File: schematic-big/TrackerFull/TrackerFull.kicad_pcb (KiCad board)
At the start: 2 copper layers, 41.1 x 61.5 mm, 59 parts, among them J1 Conn_01x05_Male, J2 MUC-20PFFR-JS7001, J3 Battery, J4 78646-3001, Q2 DMG2305UXQ, Q3 DMG2305UXQ, SW1 PTS647SK38SMTR2LFS, U2 LIS3DSH, U3 ATtiny85-20PU, U4 MCP73831-2-OT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

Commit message: schematics update
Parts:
- removed C13: 100nF, Capacitor_SMD:C_0402_1005Metric
- removed C18: 22uF, Capacitor_SMD:C_0603_1608Metric
- added U1: TLV62585PDRLR, imported:SOT50P160X60-6N, F.Cu at (191.0, 70.4)
- C17: footprint Capacitor_SMD:C_0603_1608Metric -> Capacitor_SMD:C_0805_2012Metric
- L2: value MDWK4040T3R3MM -> 1uH; footprint Inductor_SMD:L_Taiyo-Yuden_MD-4040 -> Inductor_SMD:L_Vishay_IHLP-2020
- R1: footprint Resistor_SMD:R_0805_2012Metric_Pad1.15x1.40mm_HandSolder -> Resistor_SMD:R_0603_1608Metric
- R13: value 43K -> 562K
- R14: value 10K -> 100K; footprint Resistor_SMD:R_0805_2012Metric_Pad1.15x1.40mm_HandSolder -> Resistor_SMD:R_0603_1608Metric
- moved U8 36.1 mm to (156.1, 73.0)
- moved C17 4.49 mm to (197.7, 68.7), turned to 180 degrees
- moved L2 2.67 mm to (195.7, 72.6)
- moved D3 0.73 mm to (201.2, 71.9)
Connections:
- J2 pad 1: (no net) -> /+5V
- L2 pad 1: Net-(C13-Pad1) -> Net-(L2-Pad1)
- U8 pad 1: GNDREF -> (no net)
- U8 pad 2: Net-(C13-Pad1) -> (no net)
- U8 pad 3: /+5V -> (no net)
- U8 pad 4: Net-(R13-Pad2) -> (no net)
- U8 pad 5: /+5V -> (no net)
- U8 pad 6: Net-(C13-Pad2) -> (no net)
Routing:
- net Net-(C13-Pad1): track 5.37 -> 0.00 mm
- net Net-(L2-Pad1): track 0.00 -> 4.20 mm
- net /+5V: track 67.9 -> 71.2 mm, vias 11 -> 13
- net Net-(C13-Pad2): track 1.96 -> 0.00 mm
- net /CHARGER_STAT: track 56.0 -> 56.6 mm
- net /APW_OUT: track 25.9 -> 26.5 mm
- net Net-(R13-Pad2): track 3.63 -> 4.22 mm
- net GNDREF: track 142.6 -> 142.8 mm, vias 43 -> 42

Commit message: replaced attiny
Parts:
- removed C4: 150nF, Capacitor_SMD:C_0402_1005Metric
- removed C5: 10uF, Capacitor_SMD:C_0603_1608Metric
- removed R11: 470, Resistor_SMD:R_0402_1005Metric
- removed U3: ATtiny85-20PU, Package_DIP:DIP-8_W7.62mm
- added C13: 150nF, Capacitor_SMD:C_0402_1005Metric, F.Cu at (190.1, 76.5)
- added C18: 10uF, Capacitor_SMD:C_0603_1608Metric, F.Cu at (192.6, 76.7)
- added J5: Conn_01x04_Male, Connector_PinHeader_2.54mm:PinHeader_1x04_P2.54mm_Vertical, B.Cu at (195.9, 68.4)
- added R2: 470, Resistor_SMD:R_0402_1005Metric, F.Cu at (188.3, 72.8)
- Q2, R1: moved to B.Cu
- U7: value MIC5232-2.5YD5 -> MIC5232-2.8YD5
- U8: value AP62301WU-7 -> ATtiny861A-MU; footprint Package_TO_SOT_SMD:TSOT-23-6 -> Package_DFN_QFN:QFN-32-1EP_5x5mm_P0.5mm_EP3.1x3.1mm
- moved U8 36.0 mm to (192.1, 72.7), turned to 270 degrees
- moved C16 22.6 mm to (170.0, 80.5), turned to 270 degrees
- moved U7 21.8 mm to (190.8, 88.5), turned to 0 degrees
- moved R13 21.5 mm to (171.5, 70.9), turned to 90 degrees
- moved C3 20.0 mm to (191.5, 85.8), turned to 180 degrees
- moved L2 19.5 mm to (176.3, 70.9), turned to 270 degrees
- moved C11 19.3 mm to (170.0, 68.6)
- moved U1 19.0 mm to (172.1, 68.2), turned to 180 degrees
- moved R14 18.4 mm to (171.7, 73.2), turned to 0 degrees
- moved C2 18.4 mm to (191.0, 84.4), turned to 180 degrees
- moved C19 18.4 mm to (188.0, 88.7)
- moved D3 18.2 mm to (183.2, 73.7), turned to 180 degrees
- moved R3 18.0 mm to (188.3, 74.7), turned to 270 degrees
- moved C17 17.6 mm to (180.1, 70.1), turned to 90 degrees
- moved U2 16.4 mm to (190.7, 81.8), turned to 180 degrees
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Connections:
- net /V_BAT renamed /BATTERY_IN
- R3 pad 1: /PWR_CTRL -> Net-(R3-Pad1)
- R3 pad 2: Net-(R3-Pad2) -> /LED_CTL
- U8 pad 4: (no net) -> BAT_IN
- U8 pad 5: (no net) -> GNDREF
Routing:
- net GNDREF: track 142.8 -> 88.7 mm, vias 42 -> 10
- net /CHARGER_STAT: track 56.6 -> 16.7 mm
- net /ACCEL_INT2: track 30.2 -> 0.99 mm, vias 2 -> 0
- net /AVR_RST: track 26.7 -> 0.00 mm
- net /HST_TXD: track 24.3 -> 0.00 mm
- net /LED_CTL: track 20.8 -> 0.00 mm, vias 1 -> 0
- net /HST_RXD: track 19.2 -> 0.00 mm
- net /AVR_MOSI_SDA: track 19.1 -> 0.00 mm, vias 1 -> 0
- net /SIM_RST: track 19.6 -> 0.83 mm, vias 1 -> 0
- net /VSIM: track 18.3 -> 0.25 mm, vias 2 -> 0
- net /+5V: track 71.2 -> 88.8 mm, vias 13 -> 6
- net BAT_IN: track 67.8 -> 50.6 mm, vias 5 -> 3
- net /SIM_CLK: track 16.7 -> 0.00 mm, vias 1 -> 0
- net /SIM_IO: track 14.2 -> 0.51 mm, vias 1 -> 0
- net /ACCEL_INT1: track 12.9 -> 0.72 mm
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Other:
- board size 41.1 x 61.5 mm -> 32.8 x 61.5 mm

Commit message: replaced attiny
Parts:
- C1, C19, D3, U7: moved to B.Cu
- moved J2 16.3 mm to (192.3, 66.3), turned to 0 degrees
- moved C1 13.7 mm to (192.1, 98.4), turned to 90 degrees
- moved D2 13.1 mm to (195.3, 71.7), turned to 180 degrees
- moved U7 10.1 mm to (189.3, 98.5)
- moved R8 10.1 mm to (192.4, 71.6), turned to 0 degrees
- moved C19 9.72 mm to (186.5, 98.3)
- moved R10 7.63 mm to (189.0, 71.7), turned to 180 degrees
- moved D3 7.14 mm to (177.1, 69.9), turned to 270 degrees
- moved J5 6.35 mm to (195.9, 74.7), turned to 180 degrees
- moved Q2 4.83 mm to (182.5, 73.7)
- moved SW1 3.06 mm to (190.2, 75.4)
- moved U6 2.81 mm to (188.5, 92.6)
- moved R3 2.51 mm to (186.0, 75.7)
- moved R2 2.47 mm to (186.0, 73.7)
- moved R5 2.41 mm to (189.3, 80.8), turned to 180 degrees
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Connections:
- C15 pad 1: BAT_IN -> /VBAT
- C16 pad 1: BAT_IN -> /VBAT
- D1 pad 1: (no net) -> /AVR_SCK
- D1 pad 19: /ACCEL_CS -> (no net)
- D1 pad 2: (no net) -> /AVR_MOSI_SDA
- D1 pad 20: /ACCEL_SDO -> (no net)
- D1 pad 21: /ACCEL_SDA -> (no net)
- D1 pad 22: /ACCEL_SCL -> (no net)
- D1 pad 23: /AVR_SCK -> (no net)
- D1 pad 24: /AVR_MOSI_SDA -> (no net)
- R5 pad 1: /ACCEL_CS -> Net-(R5-Pad1)
- U2 pad 4: /ACCEL_SCL -> /AVR_SCK
- U2 pad 6: /ACCEL_SDA -> /AVR_MOSI_SDA
- U2 pad 7: /ACCEL_SDO -> Net-(R5-Pad1)
- U2 pad 8: /ACCEL_CS -> Net-(R5-Pad1)
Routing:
- net /HST_TXD: track 0.00 -> 22.6 mm
- net /AVR_MOSI_SDA: track 0.00 -> 22.6 mm, vias 0 -> 4
- net /+5V: track 88.8 -> 68.0 mm
- net /AVR_SCK: track 0.00 -> 19.3 mm, vias 0 -> 1
- net /AVR_RST: track 0.00 -> 18.8 mm, vias 0 -> 1
- net GNDREF: track 88.7 -> 105.9 mm, vias 10 -> 15
- net /UART1_RXD: track 0.00 -> 16.7 mm, vias 0 -> 1
- net /HST_RXD: track 0.00 -> 16.4 mm
- net BAT_IN: track 50.6 -> 66.4 mm
- net /UART1_TXD: track 0.00 -> 15.5 mm, vias 0 -> 1
- net /ACCEL_INT1: track 0.72 -> 12.8 mm, vias 0 -> 2
- net /LED_CTL: track 0.00 -> 11.1 mm, vias 0 -> 1
- net /2.5v: track 11.7 -> 21.6 mm, vias 0 -> 1
- net /ISP_MOSI: track 0.38 -> 9.25 mm
- net /BATTERY_IN: track 23.8 -> 15.1 mm
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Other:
- board size 32.8 x 61.5 mm -> 32.8 x 60.3 mm

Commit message: pcb layout
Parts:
- removed L1: LQG15HS5N1B02, Inductor_SMD:L_0402_1005Metric
- removed L3: LQG15HS1N8B02, Inductor_SMD:L_0402_1005Metric
- removed L5: 6.2nH, Inductor_SMD:L_0402_1005Metric
- added C4: 1.2 pF, Capacitor_SMD:C_0402_1005Metric, F.Cu at (181.4, 109.5)
- added R11: 0, Resistor_SMD:R_0402_1005Metric, B.Cu at (173.0, 85.9)
- added R4: 0, Resistor_SMD:R_0402_1005Metric, F.Cu at (186.0, 69.6)
- C1, C19, U7: moved to F.Cu
- C2, C3, R5, U2: moved to B.Cu
- C20: value 0.5 pF -> 6.8 pF
- L4: value 13nF -> 6.2nH
- R10: value 10K -> 100K; footprint Resistor_SMD:R_0805_2012Metric_Pad1.15x1.40mm_HandSolder -> Resistor_SMD:R_0603_1608Metric
- moved C19 12.8 mm to (190.5, 86.1), turned to 180 degrees
- moved R6 10.9 mm to (170.2, 100.4), turned to 0 degrees
- moved U7 9.69 mm to (190.7, 88.9), turned to 270 degrees
- moved C2 7.79 mm to (188.8, 79.3), turned to 270 degrees
- moved C3 7.45 mm to (188.5, 81.3), turned to 0 degrees
- moved C1 6.80 mm to (190.6, 91.7), turned to 180 degrees
- moved C20 6.00 mm to (177.4, 109.0), turned to 180 degrees
- moved FL1 4.55 mm to (180.4, 104.9), turned to 180 degrees
- moved U2 3.82 mm to (191.3, 80.3), turned to 270 degrees
- moved C9 3.44 mm to (182.2, 106.5), turned to 0 degrees
- moved L4 3.08 mm to (179.6, 109.0), turned to 180 degrees
- moved R5 2.30 mm to (189.5, 83.1)
- moved E1 1.52 mm to (181.6, 115.2)
- moved U5 0.36 mm to (181.4, 107.5), turned to 270 degrees
- turned Q3 to 180 degrees
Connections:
- C1 pad 2: GNDREF -> GNDD
- C13 pad 1: GNDREF -> GNDD
- C13 pad 2: BAT_IN -> /LOW_CURRENT
- C18 pad 1: GNDREF -> GNDD
- C18 pad 2: BAT_IN -> /LOW_CURRENT
- C19 pad 1: BAT_IN -> /LOW_CURRENT
- C19 pad 2: GNDREF -> GNDD
- C2 pad 1: GNDREF -> GNDD
- C20 pad 2: GNDREF -> GNDD
- C3 pad 1: GNDREF -> GNDD
- C9 pad 2: GNDREF -> GNDD
- D5 pad 1: GNDREF -> GNDD
- D5 pad 3: BAT_IN -> /LOW_CURRENT
- E1 pad 2: GNDREF -> GNDD
- E1 pad 3: GNDREF -> GNDD
- E1 pad 4: GNDREF -> GNDD
- E1 pad 5: GNDREF -> GNDD
- FL1 pad 2: GNDREF -> GNDD
- FL1 pad 3: GNDREF -> GNDD
- FL1 pad 5: GNDREF -> GNDD
- J4 pad C5: GNDREF -> GNDD
- J4 pad G1: GNDREF -> GNDD
- J4 pad G2: GNDREF -> GNDD
- J4 pad G3: GNDREF -> GNDD
- J4 pad G4: GNDREF -> GNDD
- J4 pad G5: GNDREF -> GNDD
- J4 pad G6: GNDREF -> GNDD
- L4 pad 1: Net-(C20-Pad1) -> /GPS_SIGNAL
- L4 pad 2: /GPS_SIGNAL -> Net-(C20-Pad1)
- Q3 pad 2: /BATTERY_IN -> BAT_IN
- Q3 pad 3: BAT_IN -> /BATTERY_IN
- R5 pad 2: GNDREF -> GNDD
- R6 pad 1: GNDREF -> GNDD
- SW1 pad 3: GNDREF -> GNDD
- SW1 pad 4: GNDREF -> GNDD
- U2 pad 10: GNDREF -> GNDD
- U2 pad 12: GNDREF -> GNDD
- U2 pad 13: GNDREF -> GNDD
- U2 pad 16: GNDREF -> GNDD
- U2 pad 5: GNDREF -> GNDD
- U5 pad 1: GNDREF -> GNDD
- U5 pad 4: GNDREF -> GNDD
- U7 pad 1: BAT_IN -> /LOW_CURRENT
- U7 pad 2: GNDREF -> GNDD
- U7 pad 3: BAT_IN -> /LOW_CURRENT
- U8 pad 18: BAT_IN -> /LOW_CURRENT
- U8 pad 21: GNDREF -> GNDD
- U8 pad 33: GNDREF -> GNDD
- U8 pad 4: BAT_IN -> /LOW_CURRENT
- U8 pad 5: GNDREF -> GNDD
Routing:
- net GNDD: track 0.00 -> 108.4 mm, vias 0 -> 5
- net /LOW_CURRENT: track 0.00 -> 55.7 mm, vias 0 -> 2
- net BAT_IN: track 66.4 -> 21.6 mm, vias 3 -> 2
- net GNDREF: track 105.9 -> 147.5 mm, vias 15 -> 12
- net /2.5v: track 21.6 -> 47.9 mm
- net /GPS_POWER: track 1.72 -> 9.04 mm
- net /AVR_SCK: track 19.3 -> 12.5 mm
- net /GPS_RF: track 0.01 -> 5.10 mm
- net /ACCEL_INT2: track 4.73 -> 8.92 mm, vias 0 -> 1
- net /ACCEL_INT1: track 12.8 -> 8.74 mm, vias 2 -> 1
- net /AVR_MOSI_SDA: track 22.6 -> 19.4 mm, vias 4 -> 2
- net Net-(R5-Pad1): track 2.61 -> 5.64 mm
- net Net-(C20-Pad1): track 3.60 -> 1.27 mm
- net Net-(C4-Pad2): track 0.00 -> 1.98 mm
- net /GPS_SIGNAL: track 0.88 -> 2.67 mm
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- added copper zone on B.Cu, net GNDD
- removed copper zone on B.Cu, net GNDREF
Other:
- board size 32.8 x 60.3 mm -> 32.8 x 62.3 mm
- net class low_current added: clearance 0.127, trace_width 0.25, via_dia 0.5, via_drill 0.3

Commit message: pcb layout
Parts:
- removed J4: 78646-3001, imported:MOLEX_78646-3001
- added J6: 78727-0001, simcard:Molex-78727-0001-0-0-MFG, B.Cu at (172.4, 94.4)
- added Q1: DMG2305UXQ, Package_TO_SOT_SMD:SOT-23, F.Cu at (181.4, 74.2)
- added R15: 100K, Resistor_SMD:R_0603_1608Metric, F.Cu at (184.0, 72.2)
- moved R10 22.8 mm to (166.4, 69.1), turned to 90 degrees
- moved J2 16.6 mm to (198.2, 81.8), turned to 270 degrees
- moved D2 13.2 mm to (193.6, 84.8), turned to 90 degrees
- moved R8 10.4 mm to (193.9, 81.9), turned to 270 degrees
- moved J5 9.92 mm to (188.3, 68.4), turned to 270 degrees
- moved SW1 3.58 mm to (193.1, 73.3)
- moved FL1 2.55 mm to (180.1, 107.5)
- moved R6 2.29 mm to (172.5, 100.4), turned to 180 degrees
- moved U6 1.78 mm to (190.3, 92.6)
- moved C17 1.63 mm to (181.4, 71.2), turned to 0 degrees
- moved U5 1.32 mm to (181.4, 108.8)
- moved C20 1.27 mm to (177.4, 110.3)
- moved C4 1.27 mm to (181.4, 110.8)
- moved C9 1.27 mm to (182.2, 107.7)
- moved E1 1.27 mm to (181.6, 116.5)
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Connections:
- D3 pad 1: BAT_IN -> /POWER_INPUT
- Q3 pad 2: BAT_IN -> /POWER_INPUT
- R1 pad 2: GNDREF -> BAT_IN
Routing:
- net GNDREF: track 147.5 -> 95.9 mm, vias 12 -> 11
- net /SIM_DETECT_LINE: track 0.00 -> 36.2 mm, vias 0 -> 1
- net GNDD: track 108.4 -> 86.6 mm, vias 5 -> 21
- net /+5V: track 68.3 -> 88.1 mm, vias 6 -> 9
- net /POWER_INPUT: track 0.00 -> 18.8 mm, vias 0 -> 2
- net /2.5v: track 47.9 -> 64.8 mm, vias 1 -> 3
- net /GPS_POWER: track 9.04 -> 22.5 mm
- net /GPS_RF: track 5.10 -> 17.4 mm
- net /LOW_CURRENT: track 55.7 -> 43.8 mm
- net BAT_IN: track 21.6 -> 12.3 mm, vias 2 -> 3
- net /SIM_IO: track 4.30 -> 12.0 mm
- net /SIM_CLK: track 2.04 -> 6.28 mm
- net /AVR_RST: track 18.8 -> 15.0 mm
- net /ISP_MOSI: track 9.25 -> 5.51 mm
- net /SIM_RST: track 3.70 -> 6.77 mm
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- added copper zone on B.Cu, net /CHARGER_PROG
- added copper zone on F.Cu, net GNDD
- added copper zone on F.Cu, net GNDREF
- removed copper zone on F.Cu, net BAT_IN
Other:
- board size 32.8 x 62.3 mm -> 32.8 x 63.9 mm
- net class Default: via_dia 0.8 -> 0.6; via_drill 0.4 -> 0.3
- net class low_current: via_dia 0.5 -> 0.6
- net class power: via_drill 0.6 -> 0.5

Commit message: rf
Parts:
- C1, C19, U7: moved to B.Cu
- moved R17 14.9 mm to (167.4, 81.6), turned to 270 degrees
- moved C19 9.72 mm to (182.9, 92.2), turned to 90 degrees
- moved C9 9.28 mm to (176.8, 100.2), turned to 180 degrees
- moved FL1 8.85 mm to (174.7, 100.5), turned to 90 degrees
- moved U5 8.81 mm to (176.8, 101.3)
- moved R7 7.37 mm to (169.7, 81.6), turned to 90 degrees
- moved R6 7.08 mm to (179.6, 100.8)
- moved U7 6.03 mm to (185.8, 92.4), turned to 0 degrees
- moved C1 5.66 mm to (186.0, 95.0), turned to 0 degrees
- moved D1 4.95 mm to (181.7, 88.8)
- moved C8 3.81 mm to (175.3, 77.2)
- moved C10 3.81 mm to (174.3, 77.2)
- moved C14 3.81 mm to (176.6, 76.7)
- moved C12 2.67 mm to (170.0, 76.5), turned to 180 degrees
- moved Q1 2.61 mm to (182.7, 76.5), turned to 270 degrees
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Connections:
- net Net-(C4-Pad2) renamed /ANT_OUT
- net Net-(FL1-Pad1) renamed /LNA_OUTPUT
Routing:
- net GNDD: track 86.6 -> 47.1 mm, vias 21 -> 18
- net /2.5v: track 64.8 -> 42.3 mm, vias 3 -> 2
- net Net-(D1-Pad5): track 3.07 -> 23.4 mm, vias 0 -> 2
- net /GPS_RF: track 17.4 -> 0.00 mm
- net /GPS_POWER: track 22.5 -> 5.92 mm
- net /+5V: track 88.1 -> 72.8 mm
- net Net-(D1-Pad9): track 2.51 -> 11.9 mm, vias 0 -> 2
- net /GPS_SIGNAL: track 2.62 -> 11.0 mm
- net /CHARGER_STAT: track 14.1 -> 22.5 mm
- net /AVR_MOSI_SDA: track 18.6 -> 12.9 mm
- net /ACCEL_INT2: track 9.60 -> 3.89 mm
- net /HST_RXD: track 17.3 -> 11.6 mm
- net GNDREF: track 95.9 -> 90.2 mm
- net /AVR_SCK: track 15.4 -> 10.00 mm
- net /HST_TXD: track 23.6 -> 18.2 mm
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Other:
- net class RF added: clearance 0.3, trace_width 1, via_dia 0.6, via_drill 0.3

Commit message: rf
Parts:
- moved R6 12.0 mm to (168.6, 96.0), turned to 90 degrees
- moved C20 7.48 mm to (172.0, 107.5)
- moved C4 7.48 mm to (174.6, 109.3)
- moved L4 7.48 mm to (174.1, 107.6)
- moved U5 2.67 mm to (174.6, 102.7)
- moved C9 1.73 mm to (175.9, 101.7), turned to 0 degrees
- moved FL1 0.81 mm to (174.2, 101.1)
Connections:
- C9 pad 1: /2.5v -> /GPS_POWER
- U5 pad 2: /2.5v -> /GPS_POWER
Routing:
- net /GPS_POWER: track 5.92 -> 21.3 mm, vias 0 -> 2
- net /2.5v: track 42.3 -> 28.9 mm
- net GNDD: track 47.1 -> 56.0 mm, vias 18 -> 72
- net /ANT_OUT: track 2.03 -> 8.65 mm
- net /GPS_SIGNAL: track 11.0 -> 4.62 mm
- net /GPS_RF: track 0.00 -> 2.43 mm
- net /LNA_OUTPUT: track 0.00 -> 0.93 mm
- net Net-(D4-Pad2): track 2.06 -> 1.51 mm
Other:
- net class RF: clearance 0.3 -> 0.127

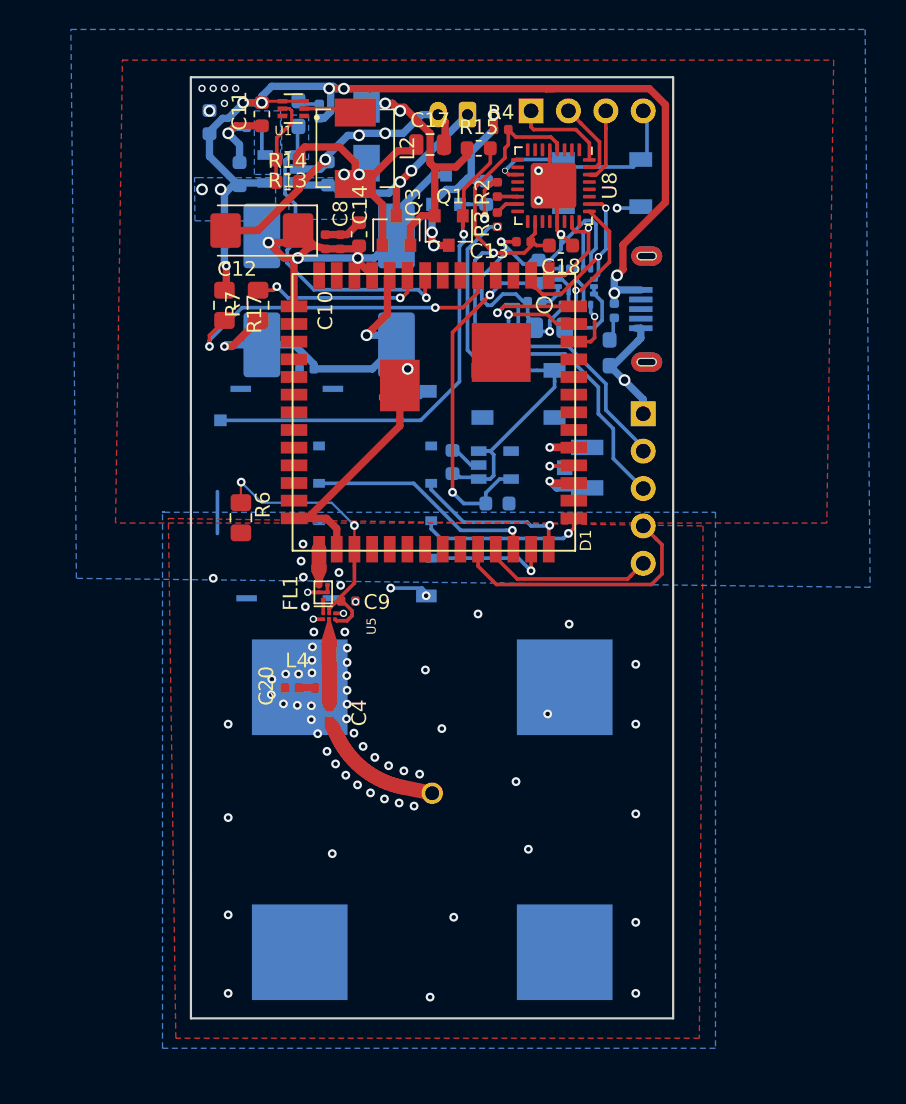
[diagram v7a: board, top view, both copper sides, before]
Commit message: attiny461 code update and new a9g footprint
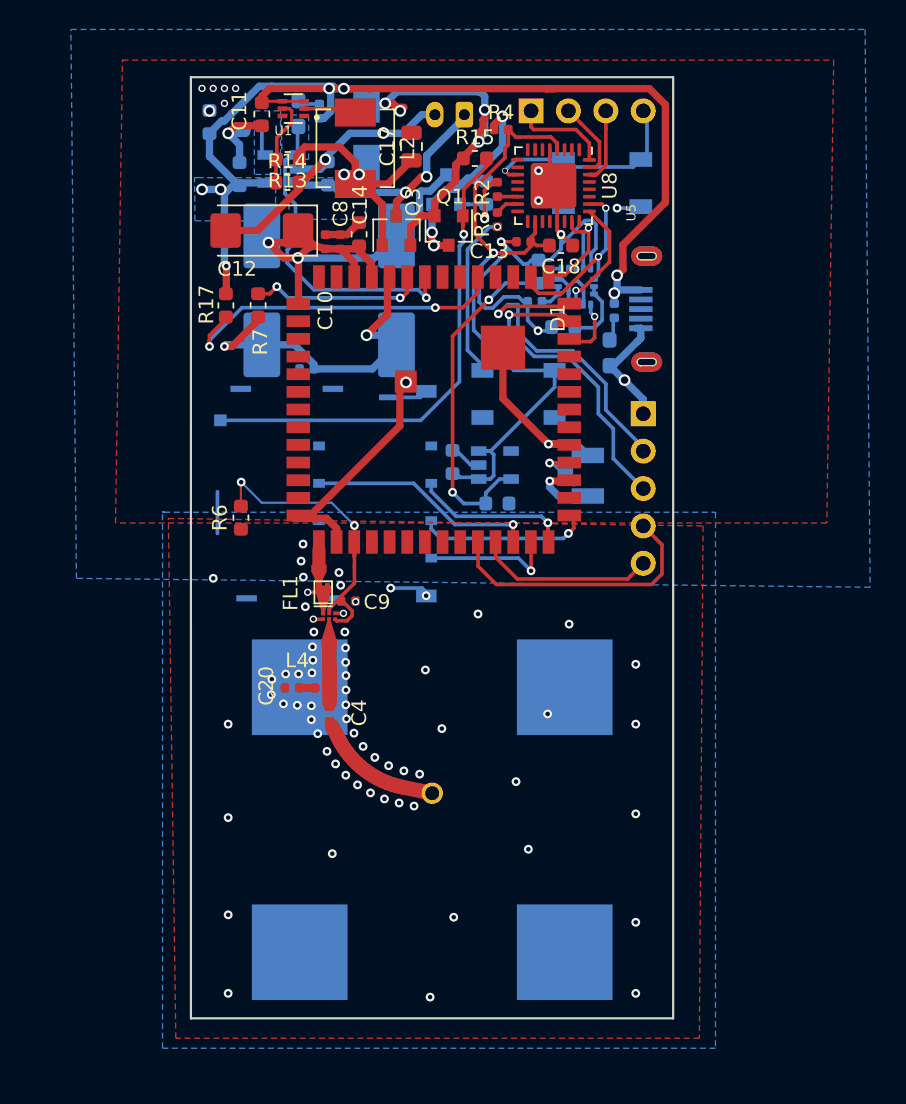
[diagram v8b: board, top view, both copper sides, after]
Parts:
- D1: footprint Tracker:A9G2 -> imported:A9
- R13: value 562K -> 56.2K
- R14: value 100K -> 10K
- R17, R5, R6, R7: footprint Resistor_SMD:R_0805_2012Metric_Pad1.15x1.40mm_HandSolder -> Resistor_SMD:R_0603_1608Metric
- moved D1 12.4 mm to (189.5, 79.2)
- moved C17 1.27 mm to (180.1, 70.8), turned to 90 degrees
- moved R5 0.92 mm to (190.5, 83.0)
- moved R15 0.74 mm to (184.5, 71.6)
- moved U6 0.55 mm to (192.1, 93.1)
- moved J3 0.22 mm to (183.7, 68.6)
- moved R17 0.10 mm to (167.5, 81.6)
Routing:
- net GNDREF: track 90.2 -> 99.2 mm, vias 11 -> 10
- net /POWER_INPUT: track 18.8 -> 25.9 mm, vias 2 -> 4
- net /+5V: track 72.8 -> 77.7 mm, vias 9 -> 7
- net /VBAT: track 31.8 -> 33.6 mm, vias 3 -> 2
- net /SIM_DETECT_LINE: track 34.9 -> 33.7 mm
- net /UART1_RXD: track 22.5 -> 21.6 mm
